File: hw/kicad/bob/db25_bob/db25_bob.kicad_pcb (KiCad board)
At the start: 2 copper layers, 99.8 x 99.8 mm, 92 parts, among them J1 DB25, J10 RJ45, J11 RJ45, J2 DB25, J3 RJ45, J4 RJ45, J5 RJ45, J6 RJ45, J7 RJ45, J8 RJ45, J9 RJ45, P1 DIL8, P10 CONN_2, P11 CONN_6, P12 CONN_4, P13 CONN_6, P14 CONN_4, P2 DIL8, P3 DIL6, P4 DIL8, P5 DIL8, P6 DIL8, P7 DIL16, P8 DIL16, P9 DIL16, Q1 FET_N, Q2 FET_N, Q3 FET_N, U1 ADuM1201WT, U10 ADuM1200CR, U11 ADuM1200CR, U12 ADuM1200CR, U13 ADuM1200CR, U14 ADuM1200CR, U2 ADuM1201WT, U3 ADuM1201WT, U4 ADuM1201WT, U5 ADuM1201WT, U6 ADuM1201WT, U7 ADuM1201WT, U8 ADuM1201WT, U9 ADuM1200CR

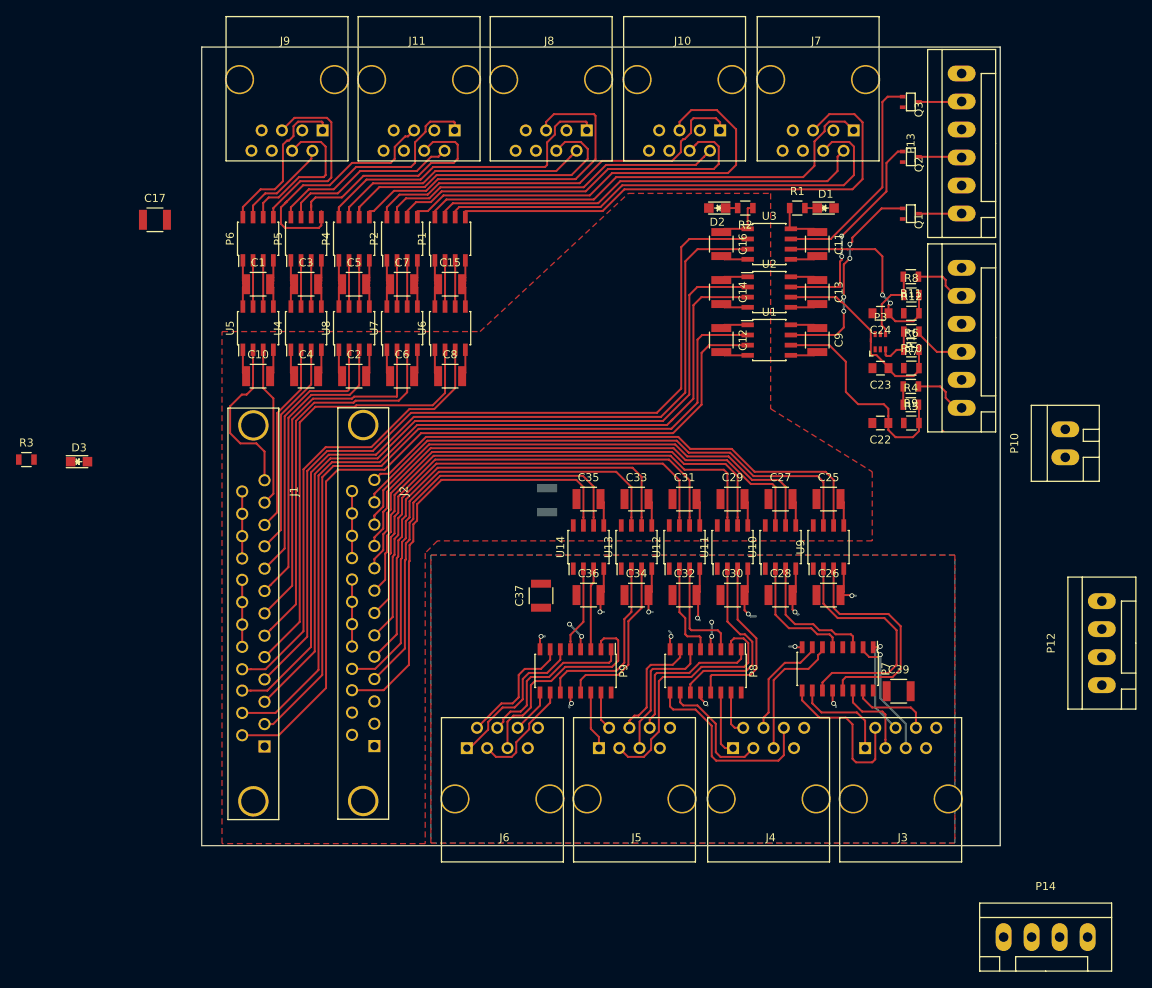
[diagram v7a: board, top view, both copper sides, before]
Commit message: Major routing done
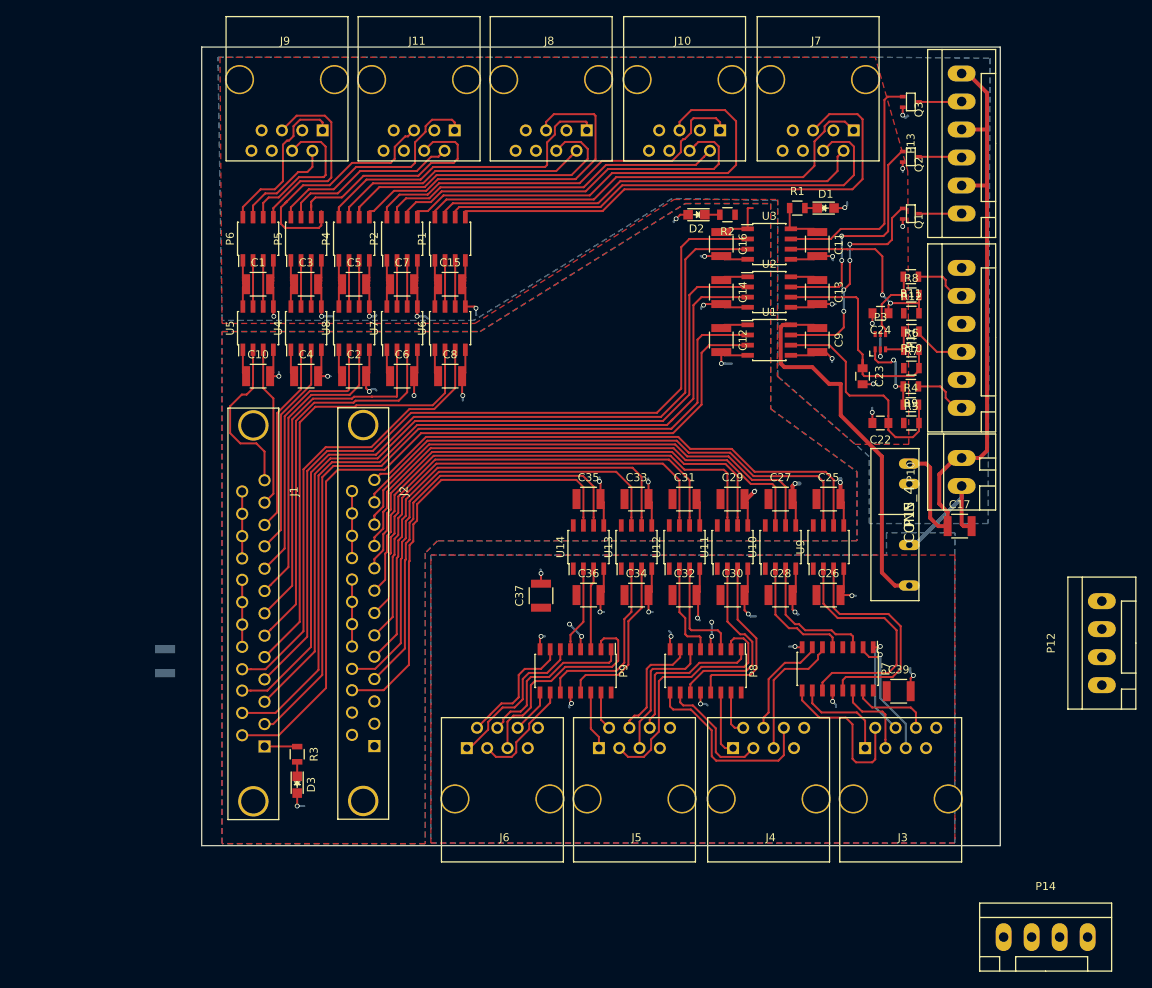
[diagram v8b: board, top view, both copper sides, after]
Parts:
- added P15: CONN_4, custom_footprints:SIP7, F.Cu at (230.4, 100.6)
- moved C17 107.6 mm to (236.7, 102.0)
- moved C38 51.8 mm to (137.4, 118.9)
- moved R3 50.0 mm to (153.9, 130.6), turned to 270 degrees
- moved D3 48.7 mm to (153.9, 134.4), turned to 270 degrees
- moved P10 13.4 mm to (237.0, 95.3)
- moved D2 2.73 mm to (203.8, 63.1)
- moved C23 2.46 mm to (224.6, 83.3), turned to 270 degrees
- moved R2 2.38 mm to (207.7, 63.1)
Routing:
- net +24V: track 0.00 -> 86.2 mm
- net EN-: track 97.6 -> 154.3 mm, vias 12 -> 30
- net +5VA: track 56.6 -> 100.9 mm
- net GND: track 65.3 -> 102.8 mm, vias 0 -> 15
- net IN0R: track 2.29 -> 10.5 mm, vias 0 -> 2
- net IN1P: track 25.3 -> 30.2 mm
- net IO16: track 0.00 -> 4.09 mm
- net OUT2: track 28.6 -> 31.5 mm
- net OUT1: track 26.6 -> 29.4 mm
- net Net-(D3-Pad1): track 0.00 -> 1.81 mm
- net OUT0: track 26.5 -> 27.8 mm
- net IN1R: track 5.64 -> 4.59 mm
- net IN2P: track 26.6 -> 25.8 mm
- net 4RX-: track 12.2 -> 12.9 mm
- net IN0P: track 28.2 -> 28.8 mm
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- added copper zone on B.Cu, net GND
